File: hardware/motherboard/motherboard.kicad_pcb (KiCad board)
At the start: 4 copper layers, 150 x 90 mm, 28 parts, among them J1 Custom_PCIe_x4, J10 Conn_01x50_MountingPin, J11 Conn_01x50_MountingPin, J12 Barrel_Jack_Switch_Pin3Ring, J2 Custom_PCIe_x4, J3 Custom_PCIe_x4, J4 Custom_PCIe_x4, J5 Custom_PCIe_x4, J6 Custom_PCIe_x4, J7 Custom_PCIe_x4, J8 Custom_PCIe_x4, J9 Conn_01x50_MountingPin, U1 74HC138, U2 TMUX1208PW, U3 SN74LV595, U5 74HC138

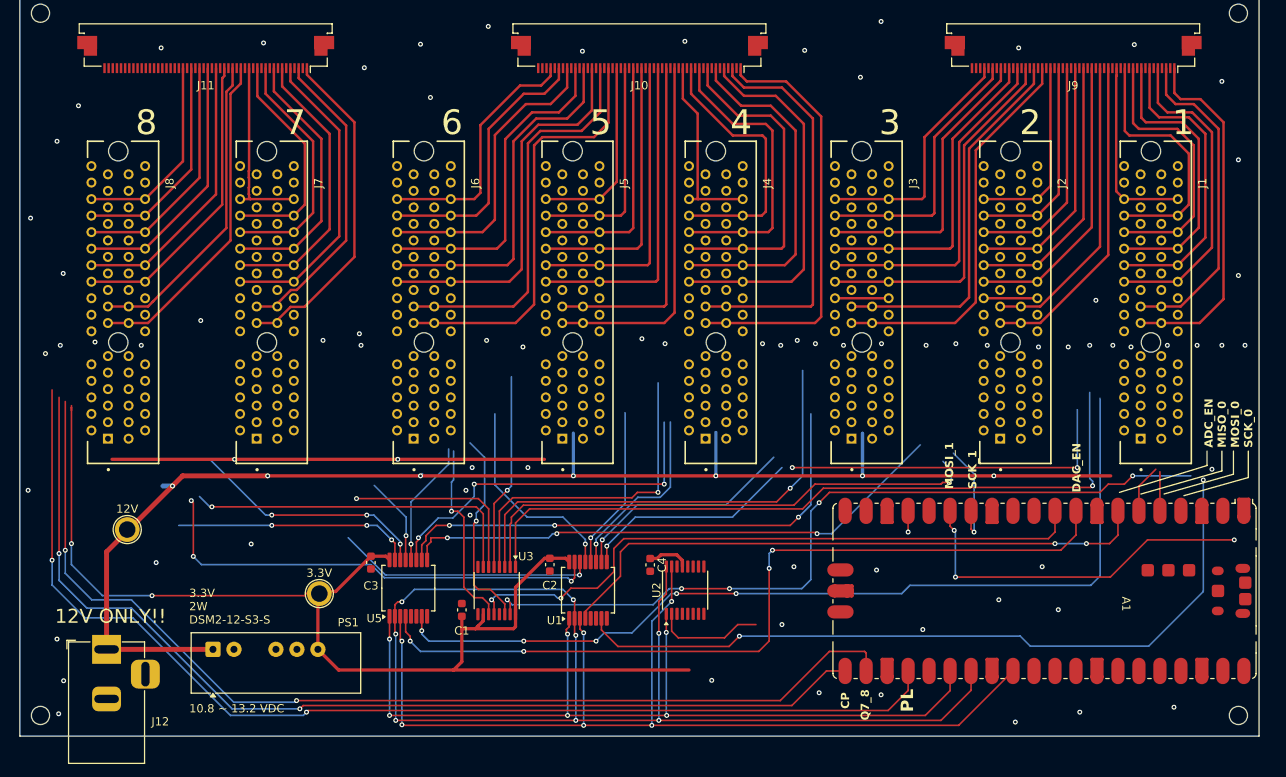
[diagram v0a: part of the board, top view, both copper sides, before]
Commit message: Respace PCIe connectors to even 18mm pitch and reroute
Place J1-J8 on an exact 18.0mm pitch centred on the board (X 82.5-232.5,
centre 157.5), replacing the previous irregular 17.0-19.0mm spacing.
Each connector moves <=1.5mm; outermost copper lands at X 88.85/226.35,
clear of the board outline.

The move severed every connector-side connection (195 track endpoints sat
on old pad positions, 0 on new ones), so the affected nets were ripped and
rerouted with the KiCad Routing Tools autorouter:

- 492 signal segments + 59 vias + 2 dangling GND segments removed
- 135 PCIe nets rerouted on F.Cu/B.Cu only, keeping In1/In2 as GND planes
- signal nets at the Default netclass 0.13mm; +3.3V/+12V at their original
  0.4mm width
- +12V additionally rerouted because its old B.Cu tracks ended up 0.27-0.33mm
  inside the moved SCK_0 pads on J3/J4/J5

Verified with check_connected.py and check_drc.py (graded at the 0.13mm
clearance actually routed to):

  connectivity  115 issues -> 0   (ALL NETS FULLY CONNECTED)
  DRC             1 -> 1          (pre-existing stray netless via at
                                   45.00,60.20, ~37mm off the left edge)

Note: +3.3V/+12V connector pads were never connected in the original board;
they are now. Routing is autorouter output intended for manual cleanup.
motherboard.kicad_pro is deliberately untouched - the router's generated
project file sets several DRC checks to "ignore" and drops
min_copper_edge_clearance to 0, so KiCad's in-GUI DRC will grade stricter
than this run did.

Co-Authored-By: Claude Opus 5 <noreply@anthropic.com>
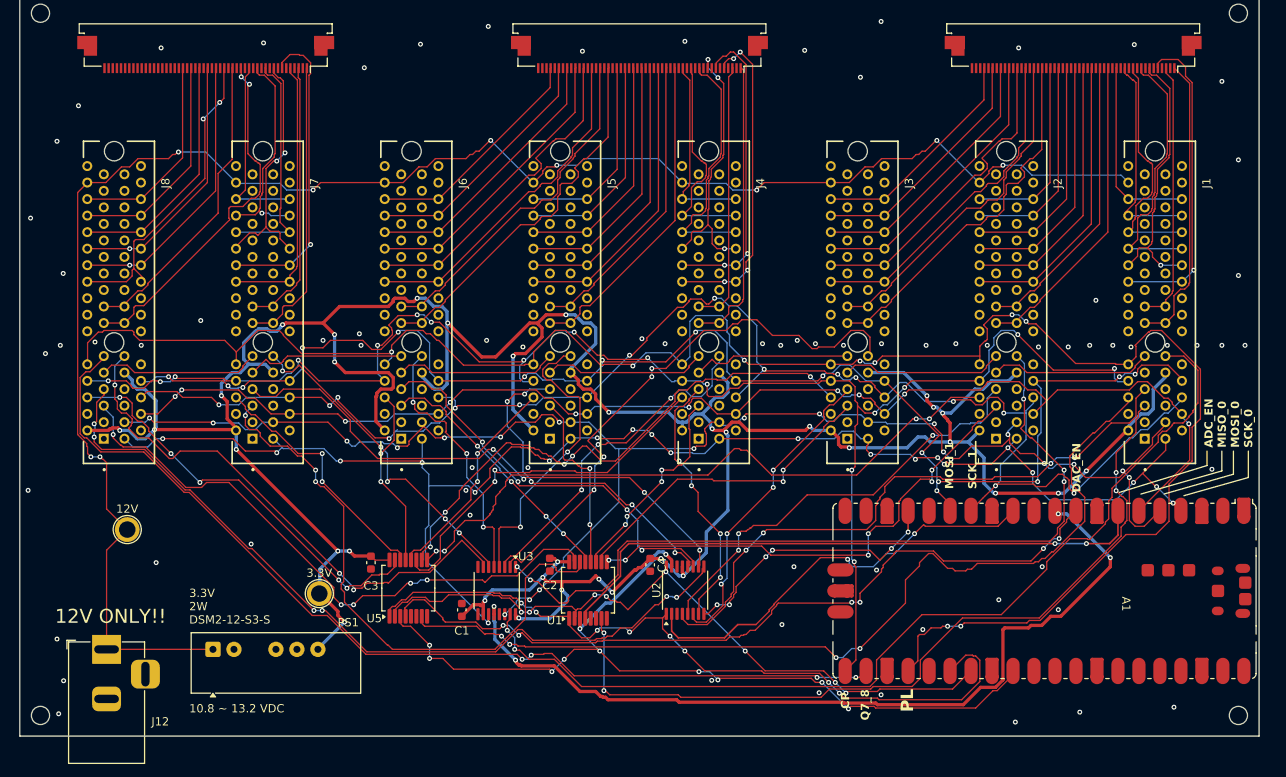
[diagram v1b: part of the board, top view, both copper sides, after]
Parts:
- moved J5 1.50 mm to (148.5, 80.0)
- moved J6 1.50 mm to (130.5, 80.0)
- moved J4 0.84 mm to (166.5, 80.0)
- moved J1 0.50 mm to (220.5, 80.0)
- moved J2 0.50 mm to (202.5, 80.0)
- moved J3 0.50 mm to (184.5, 80.0)
- moved J7 0.50 mm to (112.5, 80.0)
- moved J8 0.50 mm to (94.5, 80.0)
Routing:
- net +3.3V: track 200.9 -> 394.9 mm, vias 4 -> 35
- net SCK_1: track 13.3 -> 185.7 mm, vias 1 -> 15
- net MOSI_0: track 29.2 -> 189.6 mm, vias 1 -> 21
- net SCK_0: track 22.8 -> 182.9 mm, vias 1 -> 21
- net MISO_0: track 5.88 -> 158.1 mm, vias 0 -> 10
- net MOSI_1: track 43.9 -> 175.7 mm, vias 3 -> 15
- net PL: track 137.4 -> 236.1 mm, vias 2 -> 9
- net AT_8: track 0.00 -> 96.7 mm, vias 0 -> 6
- net AT_1: track 0.00 -> 74.5 mm, vias 0 -> 4
- net CP: track 125.7 -> 196.5 mm, vias 2 -> 17
- net AT_7: track 0.00 -> 67.0 mm, vias 0 -> 4
- net A2: track 144.1 -> 85.6 mm
- net AT_2: track 0.00 -> 52.0 mm, vias 0 -> 3
- net +12V: track 167.0 -> 216.8 mm, vias 7 -> 9
- net AT_6: track 0.00 -> 48.6 mm, vias 0 -> 4
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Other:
- board text removed: "1"
- board text removed: "2"
- board text removed: "3"
- board text removed: "4"
- board text removed: "5"
- board text removed: "6"
- board text removed: "7"
- board text removed: "8"
